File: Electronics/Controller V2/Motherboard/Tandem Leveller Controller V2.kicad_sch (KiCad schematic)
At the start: 0 parts

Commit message: Working on V2 controller. Added and laid out GNSS and valve.
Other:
- added sheet GNSS (GNSS.kicad_sch)
- added sheet Valves (Valves.kicad_sch)
- company: Copyright Britishideas.com 2026 -> (C) andy@britishideas.com 2026
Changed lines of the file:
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@@
   (title_block
     (title "Tandem Leveller Controller")
-    (date "2026-01-23")
+    (date "2026-02-02")
     (rev "V2.0")
-    (company "Copyright Britishideas.com 2026")
+    (company "(C) andy@britishideas.com 2026")
     (comment 1 "PROVIDED AS-IS, NO WARRANTY")
   )
+  (sheet (at 86.36 121.92) (size 32.385 27.94) (fields_autoplaced)
+    (stroke (width 0.1524) (type solid))
+    (fill (color 0 0 0 0.0000))
+    (property "Sheetname" "Valves" (at 86.36 121.2084 0)
+      (effects (font (size 1.27 1.27)) (justify left bottom))
+    )
+    (property "Sheetfile" "Valves.kicad_sch" (at 86.36 150.4446 0)
+      (effects (font (size 1.27 1.27)) (justify left top))
+    )
+    (pin "VALVE_A_PWM" input (at 86.36 124.46 180)
+      (effects (font (size 1.27 1.27)) (justify left))
+    )
+    (pin "VALVE_A_DIR" input (at 86.36 126.365 180)
+      (effects (font (size 1.27 1.27)) (justify left))
+    )
+    (pin "VALVE_E_PWM" input (at 86.36 145.415 180)
+      (effects (font (size 1.27 1.27)) (justify left))
+    )
+    (pin "VALVE_C_DIR" input (at 86.36 136.525 180)
+      (effects (font (size 1.27 1.27)) (justify left))
+    )
+    (pin "VALVE_D_PWM" input (at 86.36 139.7 180)
+      (effects (font (size 1.27 1.27)) (justify left))
+    )
+    (pin "VALVE_D_DIR" input (at 86.36 141.605 180)
+      (effects (font (size 1.27 1.27)) (justify left))
+    )
+    (pin "VALVE_C_PWM" input (at 86.36 134.62 180)
+      (effects (font (size 1.27 1.27)) (justify left))
+    )
+    (pin "VALVE_E_DIR" input (at 86.36 147.32 180)
+      (effects (font (size 1.27 1.27)) (justify left))
+    )
+    (pin "VALVE_B_DIR" input (at 86.36 131.445 180)
+      (effects (font (size 1.27 1.27)) (justify left))
+    )
+    (pin "VALVE_B_PWM" input (at 86.36 129.54 180)
+      (effects (font (size 1.27 1.27)) (justify left))
+    )
+    (pin "VALVE_B_MA" output (at 118.745 129.54 0)
+      (effects (font (size 1.27 1.27)) (justify right))
+    )
+    (pin "VALVE_C_MA" output (at 118.745 134.62 0)
+      (effects (font (size 1.27 1.27)) (justify right))
+    )
+    (pin "VALVE_B_MB" output (at 118.745 131.445 0)
+      (effects (font (size 1.27 1.27)) (justify right))
+    )
+    (pin "VALVE_E_MA" output (at 118.745 145.415 0)
+      (effects (font (size 1.27 1.27)) (justify right))
+    )
+    (pin "VALVE_D_MA" output (at 118.745 139.7 0)
+      (effects (font (size 1.27 1.27)) (justify right))
+    )
+    (pin "VALVE_D_MB" output (at 118.745 141.605 0)
+      (effects (font (size 1.27 1.27)) (justify right))
+    )
+    (pin "VALVE_C_MB" output (at 118.745 136.525 0)
+      (effects (font (size 1.27 1.27)) (justify right))
+    )
+    (pin "VALVE_E_MB" output (at 118.745 147.32 0)
+      (effects (font (size 1.27 1.27)) (justify right))
+    )
+    (pin "VALVE_A_MA" output (at 118.745 124.46 0)
+      (effects (font (size 1.27 1.27)) (justify right))
+    )
+    (pin "VALVE_A_MB" output (at 118.745 126.365 0)
+      (effects (font (size 1.27 1.27)) (justify right))
+    )
+    (instances
+      (project "Tandem Leveller Controller V2"
+        (path "/dceffac9-8f5b-4889-8265-b6c471cb5dde" (page "2"))
+      )
+    )
+  )
+  (sheet (at 86.36 84.455) (size 24.13 31.75) (fields_autoplaced)
+    (stroke (width 0.1524) (type solid))
+    (fill (color 0 0 0 0.0000))
+    (property "Sheetname" "GNSS" (at 86.36 83.7434 0)
+      (effects (font (size 1.27 1.27)) (justify left bottom))
+    )
+    (property "Sheetfile" "GNSS.kicad_sch" (at 86.36 116.7896 0)
+      (effects (font (size 1.27 1.27)) (justify left top))
+    )
+    (pin "GNSS_B_TX" output (at 86.36 92.075 180)
+      (effects (font (size 1.27 1.27)) (justify left))
+    )
+    (pin "GPIO_G3" bidirectional (at 86.36 111.76 180)
+      (effects (font (size 1.27 1.27)) (justify left))
+    )
+    (pin "GNSS_B_RX" input (at 86.36 93.98 180)
+      (effects (font (size 1.27 1.27)) (justify left))
+    )
+    (pin "GNSS_D_TX" output (at 86.36 102.235 180)
+      (effects (font (size 1.27 1.27)) (justify left))
+    )
+    (pin "GPIO_G2" bidirectional (at 86.36 109.855 180)
+      (effects (font (size 1.27 1.27)) (justify left))
+    )
+    (pin "GPIO_G4" bidirectional (at 86.36 113.665 180)
+      (effects (font (size 1.27 1.27)) (justify left))
+    )
+    (pin "GPIO_G1" bidirectional (at 86.36 107.95 180)
+      (effects (font (size 1.27 1.27)) (justify left))
+    )
+    (pin "GNSS_D_RX" input (at 86.36 104.14 180)
+      (effects (font (size 1.27 1.27)) (justify left))
+    )
+    (pin "GNSS_C_TX" output (at 86.36 97.155 180)
+      (effects (font (size 1.27 1.27)) (justify left))
+    )
+    (pin "GNSS_C_RX" input (at 86.36 99.06 180)
+      (effects (font (size 1.27 1.27)) (justify left))
+    )
+    (pin "GNSS_A_TX" output (at 86.36 86.995 180)
+      (effects (font (size 1.27 1.27)) (justify left))
+    )
+    (pin "GNSS_A_RX" input (at 86.36 88.9 180)
+      (effects (font (size 1.27 1.27)) (justify left))
+    )
+    (instances
+      (project "Tandem Leveller Controller V2"
+        (path "/dceffac9-8f5b-4889-8265-b6c471cb5dde" (page "3"))
+      )
+    )
+  )
   (sheet_instances

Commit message: WIP
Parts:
- added J8: Conn_01x30, symbol Connector_Generic:Conn_01x40
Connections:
- new net +5V: J8.2 (Pin_2), J8.3 (Pin_3), J8.4 (Pin_4), J8.5 (Pin_5)
- new net +BATT: J8.1 (Pin_1)
- new net CAN_H: J8.10 (Pin_10), J8.6 (Pin_6), J8.8 (Pin_8)
- new net CAN_L: J8.11 (Pin_11), J8.7 (Pin_7), J8.9 (Pin_9)
- new net GND: J8.26 (Pin_26), J8.27 (Pin_27), J8.28 (Pin_28), J8.29 (Pin_29), J8.30 (Pin_30), J8.31 (Pin_31), J8.32 (Pin_32), J8.33 (Pin_33), J8.34 (Pin_34), J8.35 (Pin_35), J8.36 (Pin_36), J8.37 (Pin_37), J8.38 (Pin_38), J8.39 (Pin_39), J8.40 (Pin_40)
- new net GPIO_C1: J8.22 (Pin_22)
- new net GPIO_C2: J8.23 (Pin_23)
- new net GPIO_C3: J8.24 (Pin_24)
- new net GPIO_C4: J8.25 (Pin_25)
- new net VALVE_A_MA: J8.12 (Pin_12)
- new net VALVE_A_MB: J8.13 (Pin_13)
- new net VALVE_B_MA: J8.14 (Pin_14)
- new net VALVE_B_MB: J8.15 (Pin_15)
- new net VALVE_C_MA: J8.16 (Pin_16)
- new net VALVE_C_MB: J8.17 (Pin_17)
- new net VALVE_D_MA: J8.18 (Pin_18)
- new net VALVE_D_MB: J8.19 (Pin_19)
- new net VALVE_E_MA: J8.20 (Pin_20)
- new net VALVE_E_MB: J8.21 (Pin_21)
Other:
- added sheet CAN (CAN.kicad_sch)
- added sheet IMU (IMU.kicad_sch)
- added sheet MCUs (MCUs.kicad_sch)
- added sheet Power (Power.kicad_sch)

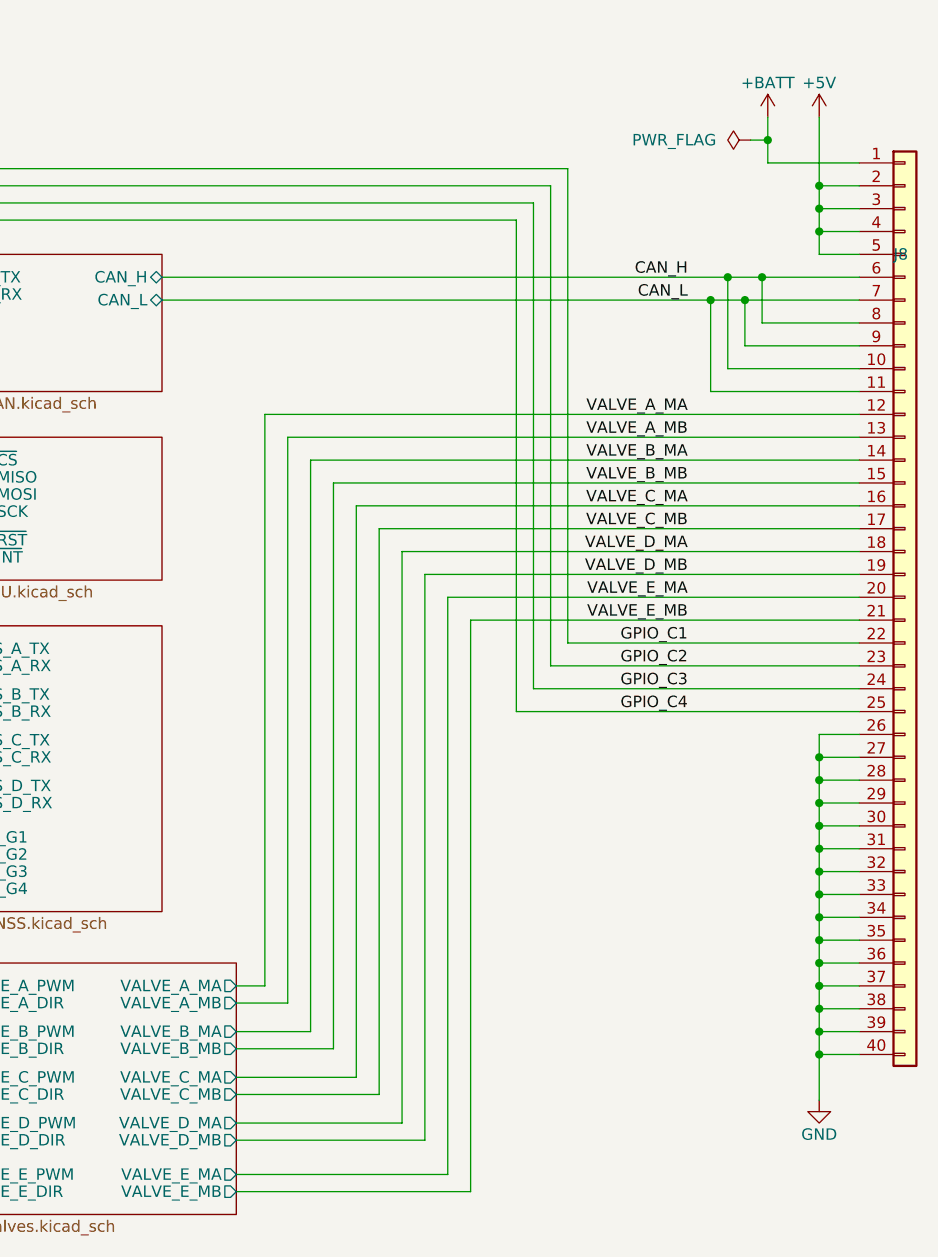
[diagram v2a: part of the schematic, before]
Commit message: Reordered main connector.
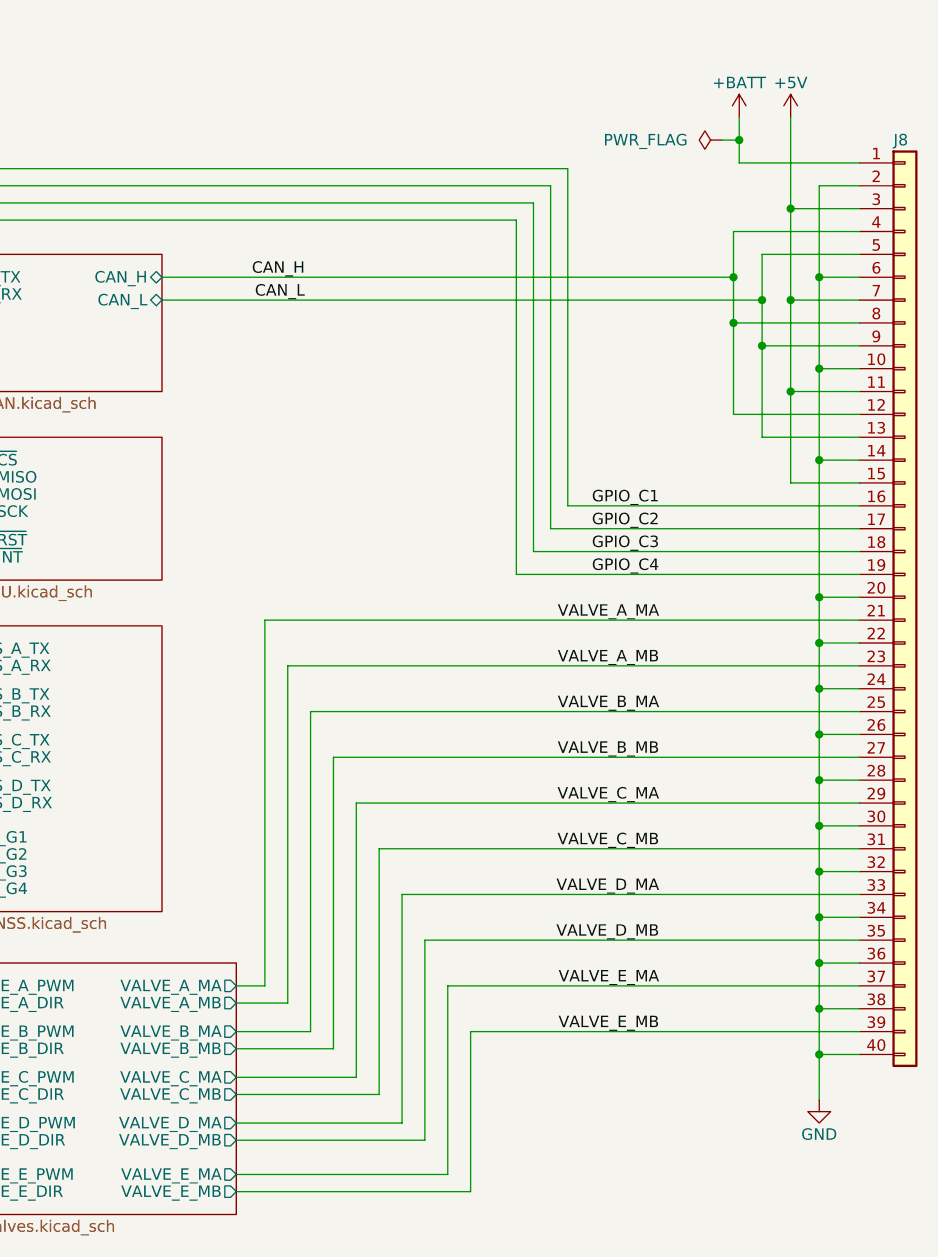
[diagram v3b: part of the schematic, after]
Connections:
- net +5V: now also J8.11 (Pin_11), J8.15 (Pin_15), J8.7 (Pin_7); no longer J8.2 (Pin_2), J8.4 (Pin_4), J8.5 (Pin_5)
- net CAN_H: now also J8.12 (Pin_12), J8.4 (Pin_4); no longer J8.10 (Pin_10), J8.6 (Pin_6)
- net CAN_L: now also J8.13 (Pin_13), J8.5 (Pin_5); no longer J8.11 (Pin_11), J8.7 (Pin_7)
- net GND: now also J8.10 (Pin_10), J8.14 (Pin_14), J8.2 (Pin_2), J8.20 (Pin_20), J8.22 (Pin_22), J8.24 (Pin_24), J8.6 (Pin_6); no longer J8.27 (Pin_27), J8.29 (Pin_29), J8.31 (Pin_31), J8.33 (Pin_33), J8.35 (Pin_35), J8.37 (Pin_37), J8.39 (Pin_39)
- net GPIO_C1: now also J8.16 (Pin_16); no longer J8.22 (Pin_22)
- net GPIO_C2: now also J8.17 (Pin_17); no longer J8.23 (Pin_23)
- net GPIO_C3: now also J8.18 (Pin_18); no longer J8.24 (Pin_24)
- net GPIO_C4: now also J8.19 (Pin_19); no longer J8.25 (Pin_25)
- net VALVE_A_MA: now also J8.21 (Pin_21); no longer J8.12 (Pin_12)
- net VALVE_A_MB: now also J8.23 (Pin_23); no longer J8.13 (Pin_13)
- net VALVE_B_MA: now also J8.25 (Pin_25); no longer J8.14 (Pin_14)
- net VALVE_B_MB: now also J8.27 (Pin_27); no longer J8.15 (Pin_15)
- net VALVE_C_MA: now also J8.29 (Pin_29); no longer J8.16 (Pin_16)
- net VALVE_C_MB: now also J8.31 (Pin_31); no longer J8.17 (Pin_17)
- net VALVE_D_MA: now also J8.33 (Pin_33); no longer J8.18 (Pin_18)
- net VALVE_D_MB: now also J8.35 (Pin_35); no longer J8.19 (Pin_19)
- net VALVE_E_MA: now also J8.37 (Pin_37); no longer J8.20 (Pin_20)
- net VALVE_E_MB: now also J8.39 (Pin_39); no longer J8.21 (Pin_21)

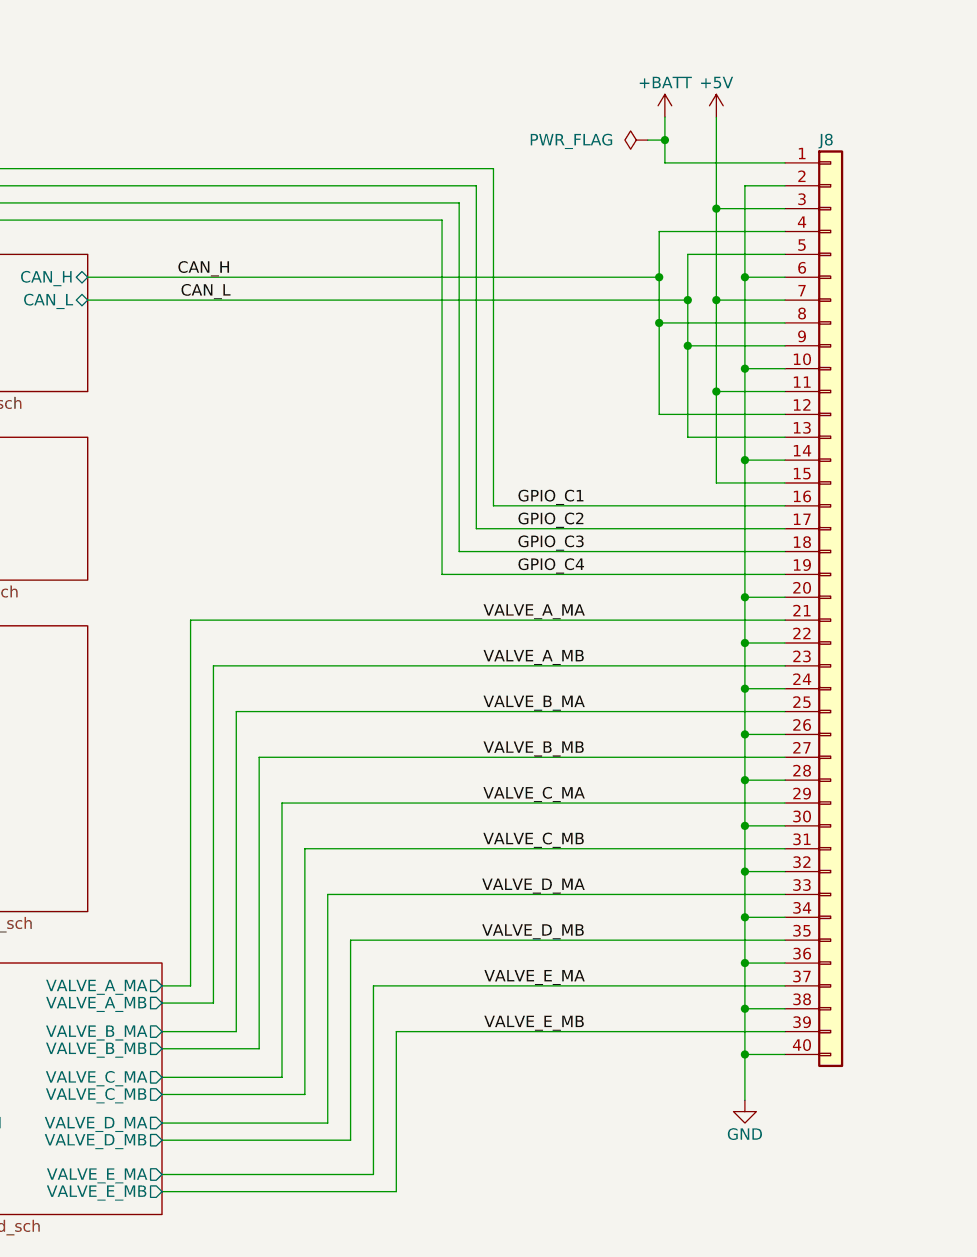
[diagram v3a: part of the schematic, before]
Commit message: Added AMP connectors. Working on PCB layout.
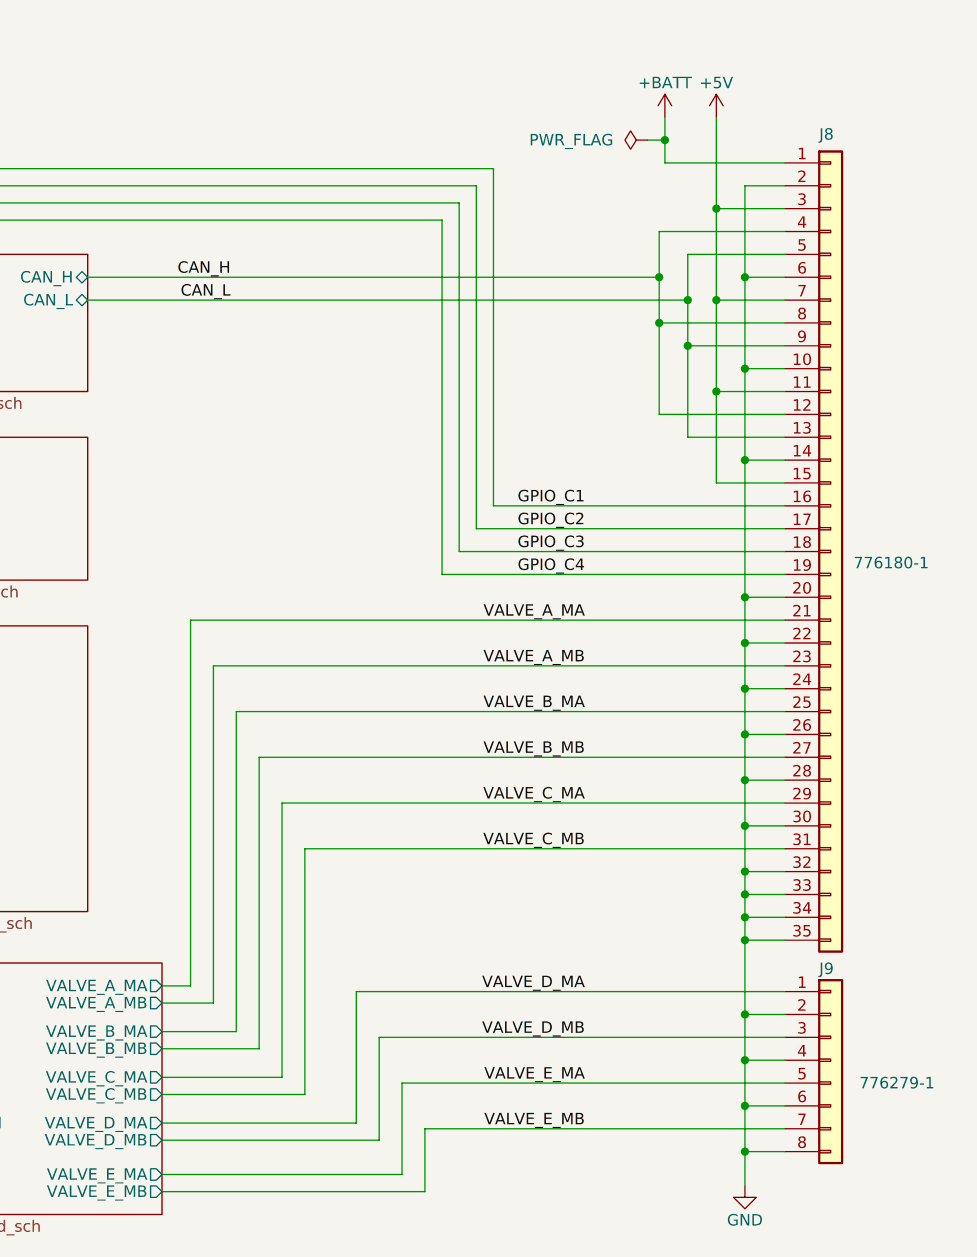
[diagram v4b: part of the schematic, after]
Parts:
- added J9: 776279-1, Britishideas:776279-1 AMPHENOL AMP 8pos, symbol Connector_Generic:Conn_01x08
- J8: value Conn_01x30 -> 776180-1; footprint (none) -> Britishideas:776180-1 AMPHENOL AMP 35pos; symbol Connector_Generic:Conn_01x40 -> Connector_Generic:Conn_01x35
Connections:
- net GND: now also J8.33 (Pin_33), J8.35 (Pin_35), J9.2 (Pin_2), J9.4 (Pin_4), J9.6 (Pin_6), J9.8 (Pin_8); no longer J8.36 (Pin_36), J8.38 (Pin_38), J8.40 (Pin_40)
- net VALVE_D_MA: now also J9.1 (Pin_1); no longer J8.33 (Pin_33)
- net VALVE_D_MB: now also J9.3 (Pin_3); no longer J8.35 (Pin_35)
- net VALVE_E_MA: now also J9.5 (Pin_5); no longer J8.37 (Pin_37)
- net VALVE_E_MB: now also J9.7 (Pin_7); no longer J8.39 (Pin_39)

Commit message: Working on V2 controller PCB.
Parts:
- added H10, H11, H12, H9: MountingHole, MountingHole:MountingHole_3.2mm_M3, symbol Mechanical:MountingHole
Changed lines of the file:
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@@
     (effects (font (size 1.27 1.27)) (justify right bottom))
+  )
+  (symbol (lib_id "Mechanical:MountingHole") (at 127 175.895 0) (unit 1)
+    (in_bom yes) (on_board yes) (dnp no) (fields_autoplaced)
+    (property "Reference" "H9" (at 129.54 174.625 0)
+      (effects (font (size 1.27 1.27)) (justify left))
+    )
+    (property "Value" "MountingHole" (at 129.54 177.165 0)
+      (effects (font (size 1.27 1.27)) (justify left))
+    )
+    (property "Footprint" "MountingHole:MountingHole_3.2mm_M3" (at 127 175.895 0)
+      (effects (font (size 1.27 1.27)) hide)
+    )
+    (property "Datasheet" "~" (at 127 175.895 0)
+      (effects (font (size 1.27 1.27)) hide)
+    )
+    (instances
+      (project "Tandem Leveller Controller V2"
+        (path "/dceffac9-8f5b-4889-8265-b6c471cb5dde"
+          (reference "H9") (unit 1)
+        )
+      )
+    )
   )
   (symbol (lib_id "Connector_Generic:Conn_01x35") (at 243.205 85.725 0) (unit 1)
@@
     )
   )
+  (symbol (lib_id "Mechanical:MountingHole") (at 127 181.61 0) (unit 1)
+    (in_bom yes) (on_board yes) (dnp no) (fields_autoplaced)
+    (property "Reference" "H10" (at 129.54 180.34 0)
+      (effects (font (size 1.27 1.27)) (justify left))
+    )
+    (property "Value" "MountingHole" (at 129.54 182.88 0)
+      (effects (font (size 1.27 1.27)) (justify left))
+    )
+    (property "Footprint" "MountingHole:MountingHole_3.2mm_M3" (at 127 181.61 0)
+      (effects (font (size 1.27 1.27)) hide)
+    )
+    (property "Datasheet" "~" (at 127 181.61 0)
+      (effects (font (size 1.27 1.27)) hide)
+    )
+    (instances
+      (project "Tandem Leveller Controller V2"
+        (path "/dceffac9-8f5b-4889-8265-b6c471cb5dde"
+          (reference "H10") (unit 1)
+        )
+      )
+    )
+  )
   (symbol (lib_id "power:PWR_FLAG") (at 222.885 40.005 90) (unit 1)
     (in_bom yes) (on_board yes) (dnp no)
@@
         (path "/dceffac9-8f5b-4889-8265-b6c471cb5dde"
           (reference "#FLG05") (unit 1)
+        )
+      )
+    )
+  )
+  (symbol (lib_id "Mechanical:MountingHole") (at 146.685 181.61 0) (unit 1)
+    (in_bom yes) (on_board yes) (dnp no) (fields_autoplaced)
+    (property "Reference" "H12" (at 149.225 180.34 0)
+      (effects (font (size 1.27 1.27)) (justify left))
+    )
+    (property "Value" "MountingHole" (at 149.225 182.88 0)
+      (effects (font (size 1.27 1.27)) (justify left))
+    )
+    (property "Footprint" "MountingHole:MountingHole_3.2mm_M3" (at 146.685 181.61 0)
+      (effects (font (size 1.27 1.27)) hide)
+    )
+    (property "Datasheet" "~" (at 146.685 181.61 0)
+      (effects (font (size 1.27 1.27)) hide)
+    )
+    (instances
+      (project "Tandem Leveller Controller V2"
+        (path "/dceffac9-8f5b-4889-8265-b6c471cb5dde"
+          (reference "H12") (unit 1)
         )
       )
@@
         )
       )
+    )
+  )
+  (symbol (lib_id "Mechanical:MountingHole") (at 146.685 175.895 0) (unit 1)
+    (in_bom yes) (on_board yes) (dnp no) (fields_autoplaced)
+    (property "Reference" "H11" (at 149.225 174.625 0)
+      (effects (font (size 1.27 1.27)) (justify left))
+    )
+    (property "Value" "MountingHole" (at 149.225 177.165 0)
+      (effects (font (size 1.27 1.27)) (justify left))
+    )
+    (property "Footprint" "MountingHole:MountingHole_3.2mm_M3" (at 146.685 175.895 0)
+      (effects (font (size 1.27 1.27)) hide)
+    )
+    (property "Datasheet" "~" (at 146.685 175.895 0)
+      (effects (font (size 1.27 1.27)) hide)
+    )
+    (instances
+      (project "Tandem Leveller Controller V2"
+        (path "/dceffac9-8f5b-4889-8265-b6c471cb5dde"
+          (reference "H11") (unit 1)
+        )
+      )
